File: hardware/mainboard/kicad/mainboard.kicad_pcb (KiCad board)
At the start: 4 copper layers, 54 x 120 mm, 166 parts, among them J1 XT30PW-M, J10 J_PYRO2, J11 J_GPS, J12 J_QWIIC, J13 J_CAM, J14 J_LED, J15 J_STACK, J16 J_SERVO4, J17 J_CHG1, J18 J_CHG2, J19 J_PYRO3, J2 J_BAT1, J20 J_PYRO4, J3 J_SW, J4 J_ARM, J5 J_SERVO1, J6 J_SERVO2, J7 J_SERVO3, J8 J_MOT, J9 J_PYRO1, Q1 AO3401A, Q2 AO3401A, Q3 AO3400A, Q4 AO3400A, Q5 AO3400A, Q6 AO3401A, Q7 AO3401A, Q8 AO3400A, Q9 AO3400A, U10 E22-400T22S, U11 MCP73831T-2ACI/OT, U12 74HC138PW, U13 74HC4051PW, U14 AP2112K-3.3TRG1, U15 BMP390, U2 TPS63070RNMR, U3 AP2112K-3.3TRG1, U4 ICM-42688-P, U5 BMP390, U6 INA239AIDGSR, U7 DRV8833PWPR, U8 SN74LV1T34DBVR

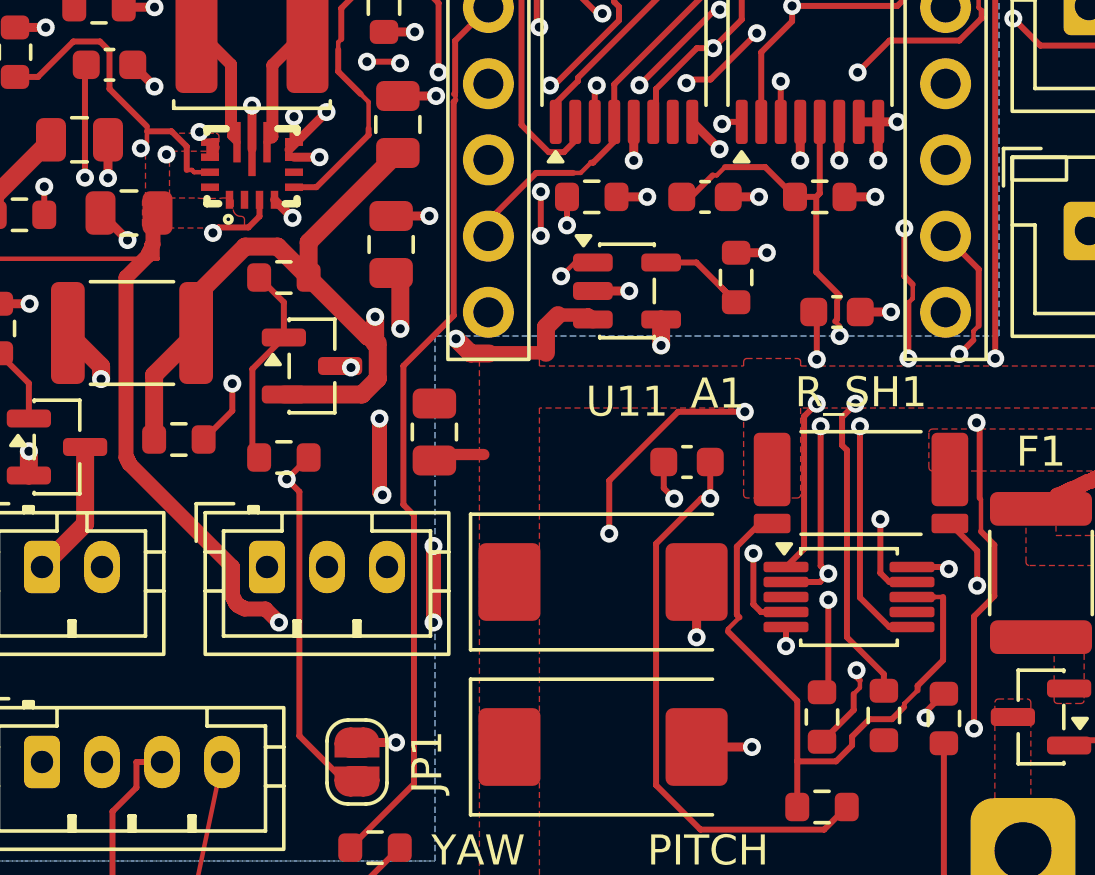
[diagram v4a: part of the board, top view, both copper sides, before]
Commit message: WIP Handrouting rev B1: GND an U6 Pad 7 und U2 Pad 15 per Via, DRC 0 Fehler / 19 offen
Beide GND-Punkte mit Stummel und Via auf In1 im KiCad-Router (Schieben) gezogen.
mainboard.kicad_pro von KiCad 10 beim Öffnen normalisiert (Netzklassen unverändert).

Co-Authored-By: Claude Opus 5.5 <noreply@anthropic.com>
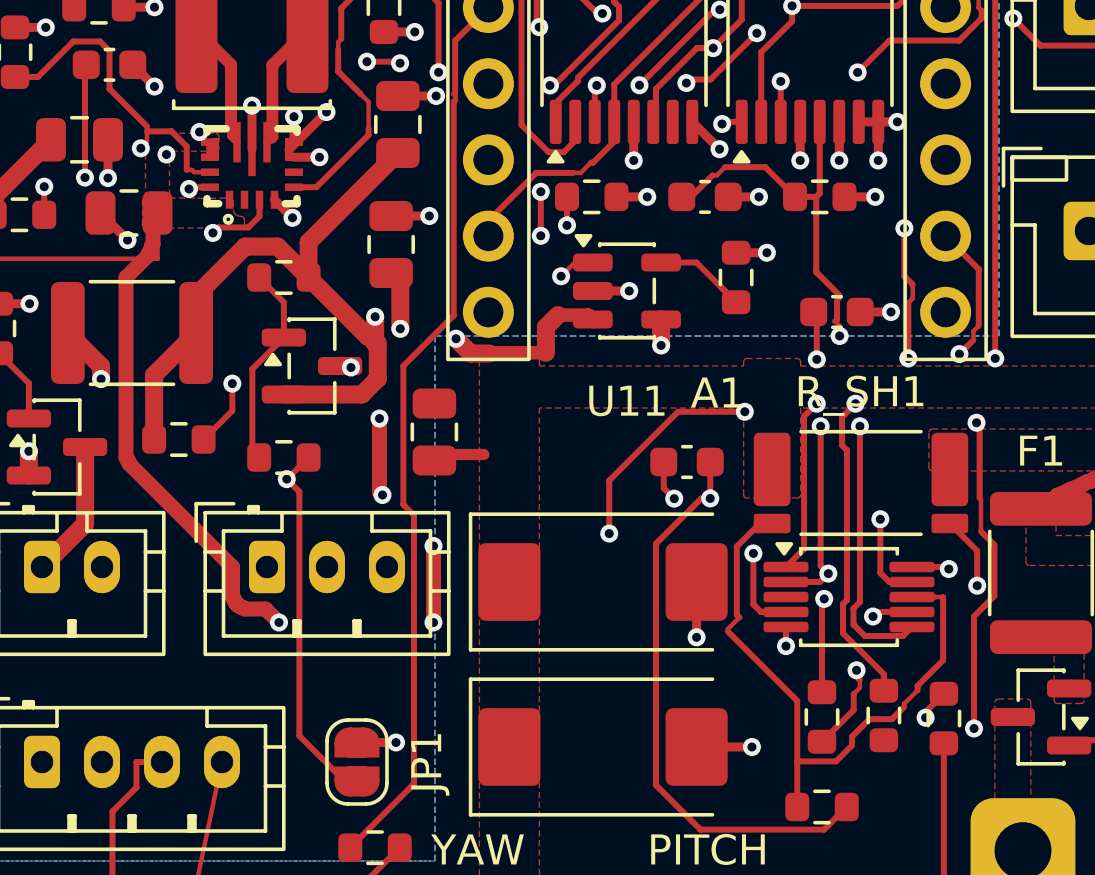
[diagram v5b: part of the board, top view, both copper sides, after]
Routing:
- net GND: track 103.3 -> 105.4 mm, vias 88 -> 90
- net 3V3: track 163.9 -> 164.9 mm
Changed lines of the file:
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@@
 	)
 	(segment
+		(start 110.1 134.54)
+		(end 109.46 134.54)
+		(width 0.2)
+		(layer "F.Cu")
+		(net "GND")
+	)
+	(segment
+		(start 133.5 148.7)
+		(end 132.35 148.7)
+		(width 0.2)
+		(layer "F.Cu")
+		(net "GND")
+	)
+	(segment
 		(start 132.53 102.79)
 		(end 133.229999 102.79)
@@
 	)
 	(segment
+		(start 132.35 148.7)
+		(end 132.2 148.85)
+		(width 0.2)
+		(layer "F.Cu")
+		(net "GND")
+	)
+	(segment
 		(start 111.25 78.35)
 		(end 112.65 78.35)
@@
 	)
 	(segment
+		(start 109.46 134.54)
+		(end 109.4 134.6)
+		(width 0.2)
+		(layer "F.Cu")
+		(net "GND")
+	)
+	(segment
 		(start 129.5 100.795)
 		(end 128.475 100.795)
@@
 	)
 	(via
+		(at 132.2 148.85)
+		(size 0.6)
+		(drill 0.3)
+		(layers "F.Cu" "B.Cu")
+		(net "GND")
+	)
+	(via
 		(at 106.075 70)
 		(size 0.6)
@@
 	)
 	(via
+		(at 109.4 134.6)
+		(size 0.6)
+		(drill 0.3)
+		(layers "F.Cu" "B.Cu")
+		(net "GND")
+	)
+	(via
 		(at 132.375 133.65)
 		(size 0.6)
@@
 	)
 	(segment
-		(start 132.7454 149.2)
-		(end 131.7655 148.2201)
+		(start 133.5 149.2)
+		(end 133.2 149.5)
+		(width 0.2)
+		(layer "F.Cu")
+		(net "3V3")
+	)
+	(segment
+		(start 131.55 148.580761)
+		(end 131.7655 148.365261)
 		(width 0.2)
 		(layer "F.Cu")
@@
 	)
 	(segment
+		(start 131.55 149.119239)
+		(end 131.55 148.580761)
+		(width 0.2)
+		(layer "F.Cu")
+		(net "3V3")
+	)
+	(segment
 		(start 149.5269 112.3377)
 		(end 149.4329 112.2437)
@@
 	)
 	(segment
-		(start 131.7655 148.2201)
-		(end 131.7655 142.5088)
-		(width 0.2)
-		(layer "F.Cu")
-		(net "3V3")
-	)
-	(segment
-		(start 133.5 149.2)
-		(end 132.7454 149.2)
-		(width 0.2)
-		(layer "F.Cu")
-		(net "3V3")
-	)
-	(segment
 		(start 120.6668 117.1368)
 		(end 119.38 115.85)
@@
 	)
 	(segment
+		(start 131.7655 148.365261)
+		(end 131.7655 142.5088)
+		(width 0.2)
+		(layer "F.Cu")
+		(net "3V3")
+	)
+	(segment
 		(start 130.3265 138.8015)
 		(end 130.3265 140.2803)
@@
 	)
 	(segment
+		(start 133.2 149.5)
+		(end 131.930761 149.5)
+		(width 0.2)
+		(layer "F.Cu")
+		(net "3V3")
+	)
+	(segment
 		(start 127.825 128.9522)
 		(end 127.825 126.6375)
@@
 	)
 	(segment
+		(start 131.930761 149.5)
+		(end 131.55 149.119239)
+		(width 0.2)
+		(layer "F.Cu")
+		(net "3V3")
+	)
+	(segment
 		(start 125.7607 123.1821)
 		(end 126.05 123.4714)
@@
 	)
 	(segment
-		(start 133.5 147.2)
-		(end 134.6602 147.2)
+		(start 130.5 148.336857)
+		(end 130.573207 148.26365)
 		(width 0.2)
 		(layer "F.Cu")
@@
 	(segment
 		(start 130.5 151.375)
-		(end 130.7103 151.1647)
+		(end 130.5 148.336857)
 		(width 0.2)
 		(layer "F.Cu")
@@
 	)
 	(segment
-		(start 130.7103 151.1647)
-		(end 130.7103 148.2935)
+		(start 133.5 147.2)
+		(end 134.6602 147.2)
 		(width 0.2)
 		(layer "F.Cu")
@@
 	)
 	(via
-		(at 130.7103 148.2935)
+		(at 130.573207 148.26365)
 		(size 0.6)
 		(drill 0.3)
@@
 	)
 	(segment
+		(start 125.5742 144.9218)
+		(end 128.9459 148.2935)
+		(width 0.2)
+		(layer "In2.Cu")
+		(net "INA_INP")
+	)
+	(segment
+		(start 134.7276 147.2674)
+		(end 133.7015 148.2935)
+		(width 0.2)
+		(layer "In2.Cu")
+		(net "INA_INP")
+	)
+	(segment
 		(start 128.9459 148.2935)
-		(end 125.5742 144.9218)
+		(end 130.543357 148.2935)
 		(width 0.2)
 		(layer "In2.Cu")
@@
 	(segment
 		(start 133.7015 148.2935)
-		(end 134.7276 147.2674)
+		(end 130.603057 148.2935)
 		(width 0.2)
 		(layer "In2.Cu")
@@
 	)
 	(segment
-		(start 130.7103 148.2935)
-		(end 133.7015 148.2935)
+		(start 130.603057 148.2935)
+		(end 130.573207 148.26365)
 		(width 0.2)
 		(layer "In2.Cu")
@@
 	)
 	(segment
-		(start 130.7103 148.2935)
-		(end 128.9459 148.2935)
+		(start 130.543357 148.2935)
+		(end 130.573207 148.26365)
 		(width 0.2)
 		(layer "In2.Cu")
@@
 	)
 	(segment
+		(start 131.2 149.4105)
+		(end 132.5625 150.773)
+		(width 0.2)
+		(layer "F.Cu")
+		(net "VBAT2_SENSE")
+	)
+	(segment
 		(start 125.825 134.8625)
 		(end 125.825 134.862)
@@
 	)
 	(segment
+		(start 131.2 148.435787)
+		(end 131.2 149.4105)
+		(width 0.2)
+		(layer "F.Cu")
+		(net "VBAT2_SENSE")
+	)
+	(segment
 		(start 126.138 134.8625)
 		(end 126.8571 134.1434)
@@
 	)
 	(segment
+		(start 131.1692 142.2052)
+		(end 131.1692 143.1438)
+		(width 0.2)
+		(layer "F.Cu")
+		(net "VBAT2_SENSE")
+	)
+	(segment
 		(start 130.3079 137.3688)
 		(end 131.0882 138.1491)
@@
 	)
 	(segment
-		(start 132.5625 150.773)
-		(end 132.5625 151.325)
+		(start 131.3319 148.303886)
+		(end 131.2 148.435787)
 		(width 0.2)
 		(layer "F.Cu")
@@
 	)
 	(segment
+		(start 131.6174 141.757)
+		(end 131.1692 142.2052)
+		(width 0.2)
+		(layer "F.Cu")
+		(net "VBAT2_SENSE")
+	)
+	(segment
 		(start 129.6 134.8625)
 		(end 130.3079 134.8625)
@@
 	)
 	(segment
-		(start 131.6174 141.757)
-		(end 131.1692 142.2052)
+		(start 131.1692 143.1438)
+		(end 131.3319 143.3065)
 		(width 0.2)
 		(layer "F.Cu")
@@
 	)
 	(segment
-		(start 131.3319 149.5424)
-		(end 132.5625 150.773)
+		(start 131.3319 143.3065)
+		(end 131.3319 148.303886)
 		(width 0.2)
 		(layer "F.Cu")
@@
 	)
 	(segment
-		(start 131.1692 143.1438)
-		(end 131.3319 143.3065)
+		(start 132.5625 150.773)
+		(end 132.5625 151.325)
 		(width 0.2)
 		(layer "F.Cu")
@@
 		(layer "F.Cu")
 		(net "VBAT2_SENSE")
-	)
-	(segment
-		(start 131.1692 142.2052)
-		(end 131.1692 143.1438)
-		(width 0.2)
-		(layer "F.Cu")
-		(net "VBAT2_SENSE")
-	)
-	(segment
-		(start 131.3319 143.3065)
-		(end 131.3319 149.5424)
-		(width 0.2)
-		(layer "F.Cu")
-		(net "VBAT2_SENSE")
